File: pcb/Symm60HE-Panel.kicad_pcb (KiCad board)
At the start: 2 copper layers, 175.3 x 233.9 mm, 310 parts

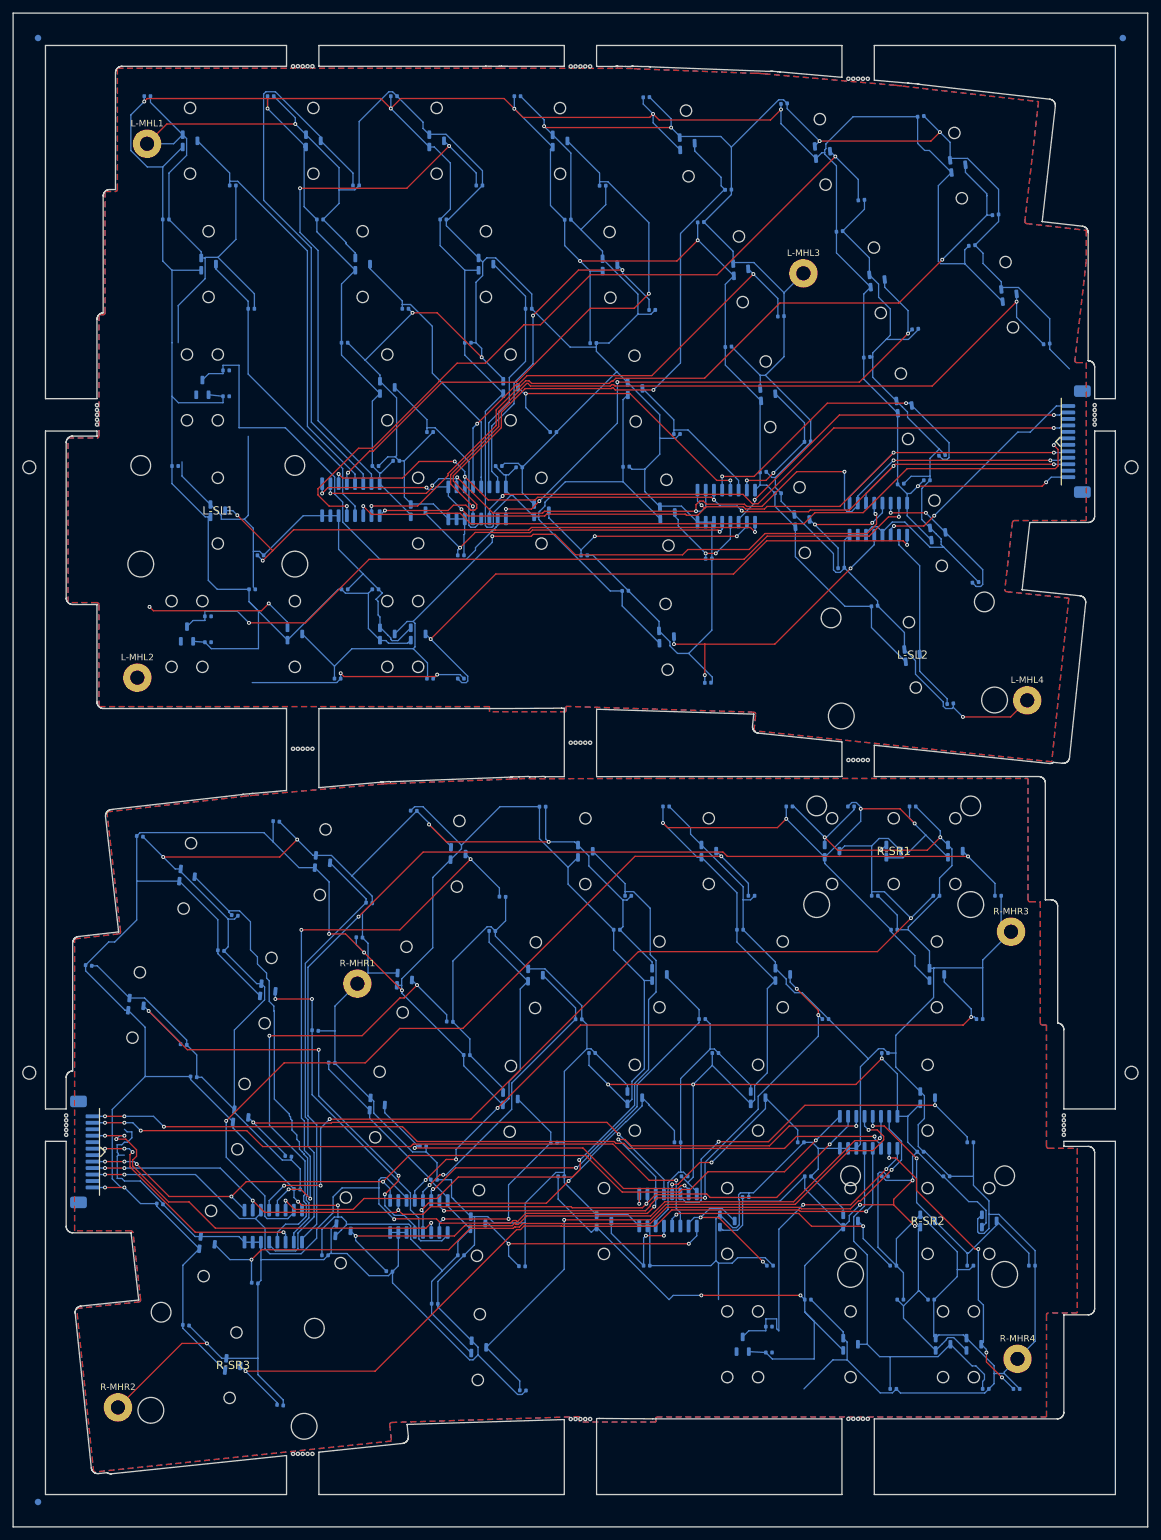
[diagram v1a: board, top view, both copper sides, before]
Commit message: Replace the project with the reorganised T7 tree: ribbon keyboard is production, pogo archived
Production design is now the outward-facing FPC keyboard with per-key
SK6812MINI-E reverse-mount LEDs, a fifth SN74LV4051A mux per half so every
alternate Hall position has its own channel, an SN74AHCT1G125 LED level
shifter, a 50 x 31 mm daughterboard, 1.5 mm POM plates and 3 degree / 7 degree
tent and typing angles. The universal half panel is fully populated (359
placements) with routed NPTH alignment slots for the mutually exclusive
positions, and eight fixed-layout Left/Right PCB pairs are released under
release/layout-pcbs/ with matching BOM, CPL, Gerber ZIP, drill report and DRC.

Reorganise tools/ into cad/, generators/, layouts/, pcb/, pogo/, releases/ and
rendering/ subpackages; add designs/ and layout/ (KLE) trees and per-layout
gallery renders. The Fusion handoff is a fourteen-body reference STEP with
Gateron KS-20 switch and Cherry-profile keycap references and exact BOOMELE,
HRO and XKB models under case/fusion360/models/official/ with provenance.

The Neo-style pogo variant, its Mill-Max vendor models, the Fusion setup
script and the pogo release packages are archived as design history and
marked DO-NOT-ORDER. Their restored BOM snapshots had reintroduced the wrong
mux part C7792; corrected to C128414 / SN74LV4051ADR and their checksum lists
and archives rebuilt.

Co-Authored-By: Claude Opus 5 <noreply@anthropic.com>
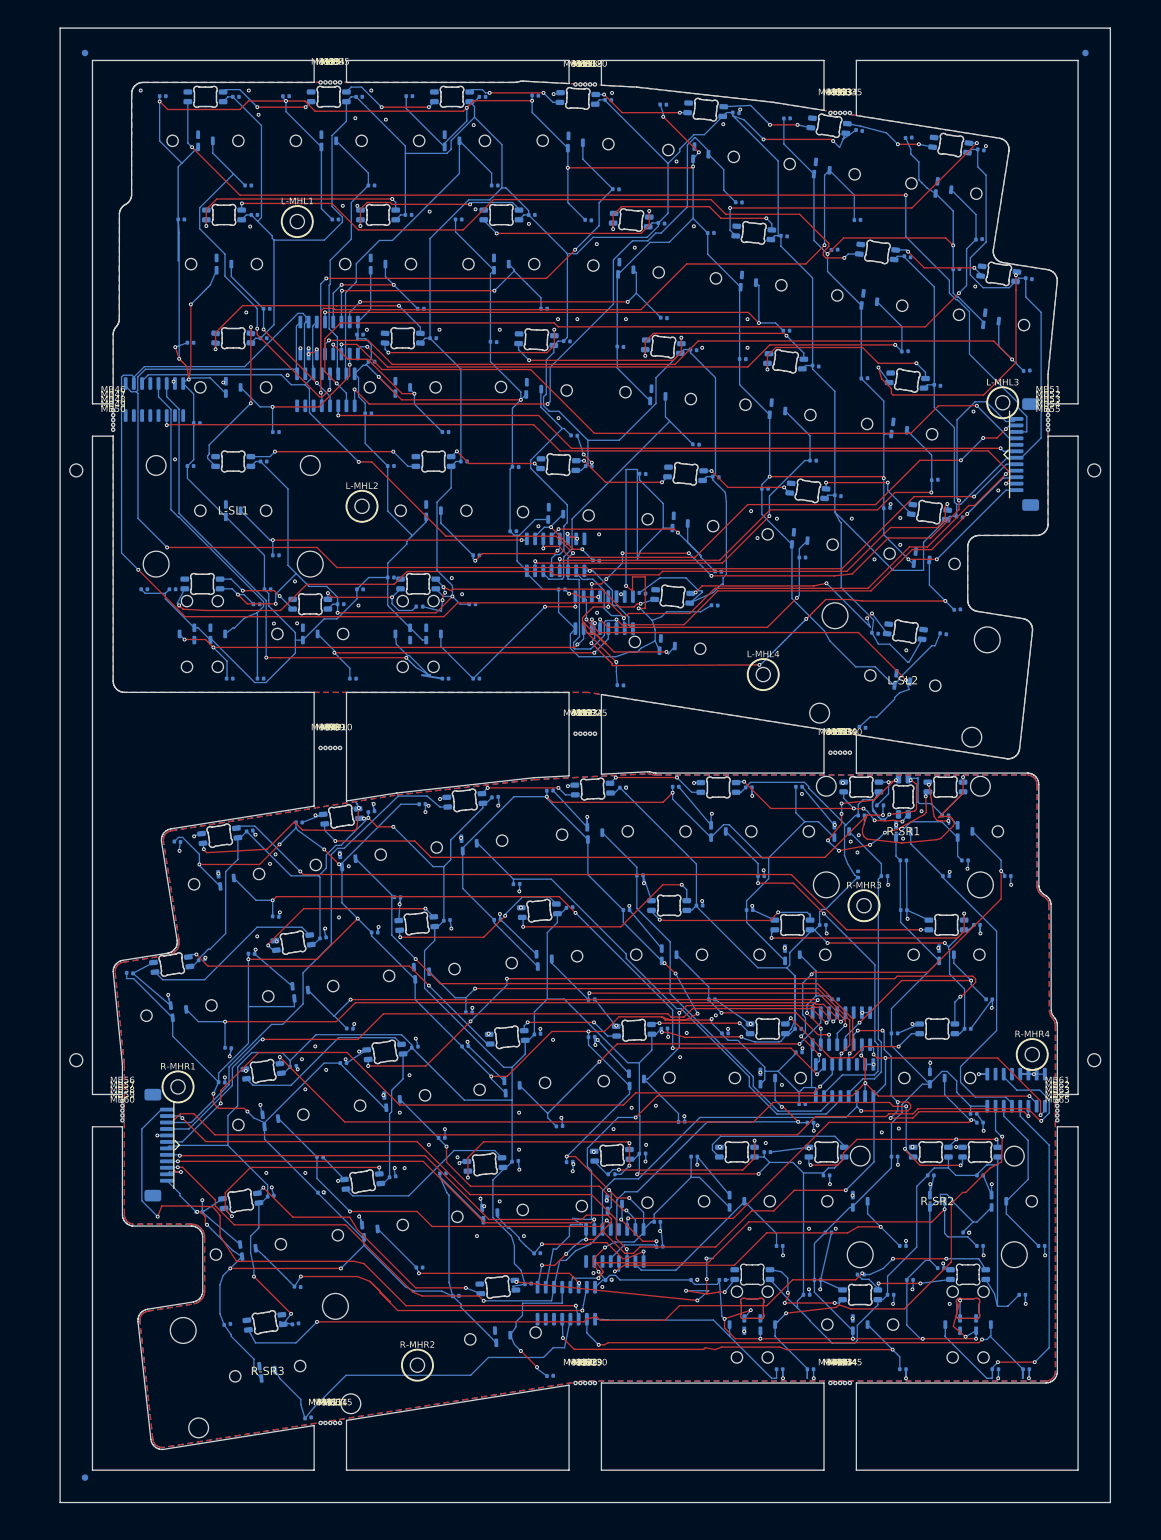
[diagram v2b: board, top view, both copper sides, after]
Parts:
- removed L-KML15N, L-KML15S, L-KML27A, L-KML27N, R-KMR30A, R-KMR30N: MX_MECHANICAL_ONLY, HE_KEY_MECHANICAL_ONLY
- added L-AML5: SN74LV4051A, Symm60HE_Project:AM1_SOIC-16_3.9x9.9mm_P1.27mm, B.Cu at (5.92, 49.5)
- added L-CL28A: 100n, Symm60HE_Project:C1_C_0402_1005Metric, B.Cu at (8.71, 78.8)
- added L-CL28B: 4.7n, Symm60HE_Project:C1_C_0402_1005Metric, B.Cu at (22.3, 92.6)
- added L-CML5: 100n, Symm60HE_Project:C1_C_0402_1005Metric, B.Cu at (12.5, 53.1)
- added L-CRGBL1: 100n, Symm60HE_Project:C1_C_0402_1005Metric, B.Cu at (18.5, 2.73)
- added L-CRGBL10: 100n, Symm60HE_Project:C1_C_0402_1005Metric, B.Cu at (64.2, 21.0)
- added L-CRGBL11: 100n, Symm60HE_Project:C1_C_0402_1005Metric, B.Cu at (45.2, 21.0)
- added L-CRGBL12: 100n, Symm60HE_Project:C1_C_0402_1005Metric, B.Cu at (21.4, 21.0)
- added L-CRGBL13: 100n, Symm60HE_Project:C1_C_0402_1005Metric, B.Cu at (122.3, 27.4)
- added L-CRGBL14: 100n, Symm60HE_Project:C1_C_0402_1005Metric, B.Cu at (141.0, 30.8)
- added L-CRGBL15: 100n, Symm60HE_Project:C1_C_0402_1005Metric, B.Cu at (126.9, 47.3)
- added L-CRGBL16: 100n, Symm60HE_Project:C1_C_0402_1005Metric, B.Cu at (108.1, 44.3)
- added L-CRGBL17: 100n, Symm60HE_Project:C1_C_0402_1005Metric, B.Cu at (89.2, 41.8)
- added L-CRGBL18: 100n, Symm60HE_Project:C1_C_0402_1005Metric, B.Cu at (69.6, 40.5)
- added L-CRGBL19: 100n, Symm60HE_Project:C1_C_0402_1005Metric, B.Cu at (49.0, 40.0)
- added L-CRGBL2: 100n, Symm60HE_Project:C1_C_0402_1005Metric, B.Cu at (37.6, 2.73)
- added L-CRGBL20: 100n, Symm60HE_Project:C1_C_0402_1005Metric, B.Cu at (22.8, 40.0)
- added L-CRGBL21: 100n, Symm60HE_Project:C1_C_0402_1005Metric, B.Cu at (22.8, 59.1)
- added L-CRGBL22: 100n, Symm60HE_Project:C1_C_0402_1005Metric, B.Cu at (53.8, 59.1)
- added L-CRGBL23: 100n, Symm60HE_Project:C1_C_0402_1005Metric, B.Cu at (73.0, 59.8)
- added L-CRGBL24: 100n, Symm60HE_Project:C1_C_0402_1005Metric, B.Cu at (92.7, 61.5)
- added L-CRGBL25: 100n, Symm60HE_Project:C1_C_0402_1005Metric, B.Cu at (111.5, 64.4)
- added L-CRGBL26: 100n, Symm60HE_Project:C1_C_0402_1005Metric, B.Cu at (130.3, 67.6)
- added L-CRGBL27: 100n, Symm60HE_Project:C1_C_0402_1005Metric, B.Cu at (21.7, 81.1)
- added L-CRGBL29: 100n, Symm60HE_Project:C1_C_0402_1005Metric, B.Cu at (55.1, 81.1)
- added L-CRGBL3: 100n, Symm60HE_Project:C1_C_0402_1005Metric, B.Cu at (56.6, 2.73)
- added L-CRGBL30: 100n, Symm60HE_Project:C1_C_0402_1005Metric, B.Cu at (81.3, 79.4)
- added L-CRGBL31: 100n, Symm60HE_Project:C1_C_0402_1005Metric, B.Cu at (117.3, 85.6)
- added L-CRGBL33: 100n, Symm60HE_Project:C1_C_0402_1005Metric, B.Cu at (34.7, 81.1)
- added L-CRGBL4: 100n, Symm60HE_Project:C1_C_0402_1005Metric, B.Cu at (76.0, 3.22)
- added L-CRGBL5: 100n, Symm60HE_Project:C1_C_0402_1005Metric, B.Cu at (95.8, 5.21)
- added L-CRGBL6: 100n, Symm60HE_Project:C1_C_0402_1005Metric, B.Cu at (114.8, 7.93)
- added L-CRGBL7: 100n, Symm60HE_Project:C1_C_0402_1005Metric, B.Cu at (133.6, 10.9)
- added L-CRGBL8: 100n, Symm60HE_Project:C1_C_0402_1005Metric, B.Cu at (103.2, 24.2)
- added L-CRGBL9: 100n, Symm60HE_Project:C1_C_0402_1005Metric, B.Cu at (84.3, 22.3)
- added L-DL1: SK6812MINI-E, Symm60HE_Project:SK6812MINI-E_ReverseMount, B.Cu at (13.8, 2.73)
- added L-DL10: SK6812MINI-E, Symm60HE_Project:SK6812MINI-E_ReverseMount, B.Cu at (59.5, 21.0)
- added L-DL11: SK6812MINI-E, Symm60HE_Project:SK6812MINI-E_ReverseMount, B.Cu at (40.5, 21.0)
- added L-DL12: SK6812MINI-E, Symm60HE_Project:SK6812MINI-E_ReverseMount, B.Cu at (16.7, 21.0)
- added L-DL13: SK6812MINI-E, Symm60HE_Project:SK6812MINI-E_ReverseMount, B.Cu at (117.6, 26.7)
- added L-DL14: SK6812MINI-E, Symm60HE_Project:SK6812MINI-E_ReverseMount, B.Cu at (136.4, 30.1)
- added L-DL15: SK6812MINI-E, Symm60HE_Project:SK6812MINI-E_ReverseMount, B.Cu at (122.3, 46.6)
- added L-DL16: SK6812MINI-E, Symm60HE_Project:SK6812MINI-E_ReverseMount, B.Cu at (103.5, 43.6)
- added L-DL17: SK6812MINI-E, Symm60HE_Project:SK6812MINI-E_ReverseMount, B.Cu at (84.6, 41.3)
- added L-DL18: SK6812MINI-E, Symm60HE_Project:SK6812MINI-E_ReverseMount, B.Cu at (65.0, 40.2)
- added L-DL19: SK6812MINI-E, Symm60HE_Project:SK6812MINI-E_ReverseMount, B.Cu at (44.3, 40.0)
- added L-DL2: SK6812MINI-E, Symm60HE_Project:SK6812MINI-E_ReverseMount, B.Cu at (32.9, 2.73)
- added L-DL20: SK6812MINI-E, Symm60HE_Project:SK6812MINI-E_ReverseMount, B.Cu at (18.1, 40.0)
- added L-DL21: SK6812MINI-E, Symm60HE_Project:SK6812MINI-E_ReverseMount, B.Cu at (18.1, 59.1)
- added L-DL22: SK6812MINI-E, Symm60HE_Project:SK6812MINI-E_ReverseMount, B.Cu at (49.1, 59.1)
- added L-DL23: SK6812MINI-E, Symm60HE_Project:SK6812MINI-E_ReverseMount, B.Cu at (68.3, 59.6)
- added L-DL24: SK6812MINI-E, Symm60HE_Project:SK6812MINI-E_ReverseMount, B.Cu at (88.0, 61.0)
- added L-DL25: SK6812MINI-E, Symm60HE_Project:SK6812MINI-E_ReverseMount, B.Cu at (106.9, 63.6)
- added L-DL26: SK6812MINI-E, Symm60HE_Project:SK6812MINI-E_ReverseMount, B.Cu at (125.7, 66.9)
- added L-DL27: SK6812MINI-E, Symm60HE_Project:SK6812MINI-E_ReverseMount, B.Cu at (13.3, 78.0)
- added L-DL29: SK6812MINI-E, Symm60HE_Project:SK6812MINI-E_ReverseMount, B.Cu at (46.7, 78.0)
- added L-DL3: SK6812MINI-E, Symm60HE_Project:SK6812MINI-E_ReverseMount, B.Cu at (51.9, 2.73)
- added L-DL30: SK6812MINI-E, Symm60HE_Project:SK6812MINI-E_ReverseMount, B.Cu at (86.0, 79.9)
- added L-DL31: SK6812MINI-E, Symm60HE_Project:SK6812MINI-E_ReverseMount, B.Cu at (122.0, 85.4)
- added L-DL33: SK6812MINI-E, Symm60HE_Project:SK6812MINI-E_ReverseMount, B.Cu at (30.0, 81.1)
- added L-DL4: SK6812MINI-E, Symm60HE_Project:SK6812MINI-E_ReverseMount, B.Cu at (71.4, 2.98)
- added L-DL5: SK6812MINI-E, Symm60HE_Project:SK6812MINI-E_ReverseMount, B.Cu at (91.1, 4.72)
- added L-DL6: SK6812MINI-E, Symm60HE_Project:SK6812MINI-E_ReverseMount, B.Cu at (110.2, 7.19)
- added L-DL7: SK6812MINI-E, Symm60HE_Project:SK6812MINI-E_ReverseMount, B.Cu at (129.0, 10.2)
- added L-DL8: SK6812MINI-E, Symm60HE_Project:SK6812MINI-E_ReverseMount, B.Cu at (98.5, 23.8)
- added L-DL9: SK6812MINI-E, Symm60HE_Project:SK6812MINI-E_ReverseMount, B.Cu at (79.6, 21.8)
- added L-HEL28: MT9102ET, HE_KEY_1.50u, B.Cu at (15.7, 85.7)
- added L-RBPL29: 0R_DNP, Symm60HE_Project:R3_R_0402_1005Metric, B.Cu at (46.9, 81.5)
- added R-AMR5: SN74LV4051A, Symm60HE_Project:AM1_SOIC-16_3.9x9.9mm_P1.27mm, B.Cu at (139.1, 156.2)
- added R-CMR5: 100n, Symm60HE_Project:C1_C_0402_1005Metric, B.Cu at (132.5, 159.9)
- added R-CR31A: 100n, Symm60HE_Project:C1_C_0402_1005Metric, B.Cu at (93.7, 185.5)
- added R-CR31B: 4.7n, Symm60HE_Project:C1_C_0402_1005Metric, B.Cu at (107.3, 199.3)
- added R-CRGBR1: 100n, Symm60HE_Project:C1_C_0402_1005Metric, B.Cu at (58.6, 110.9)
- added R-CRGBR10: 100n, Symm60HE_Project:C1_C_0402_1005Metric, B.Cu at (90.2, 127.7)
- added R-CRGBR11: 100n, Symm60HE_Project:C1_C_0402_1005Metric, B.Cu at (70.1, 128.0)
- added R-CRGBR12: 100n, Symm60HE_Project:C1_C_0402_1005Metric, B.Cu at (51.1, 130.0)
- added R-CRGBR13: 100n, Symm60HE_Project:C1_C_0402_1005Metric, B.Cu at (32.0, 132.7)
- added R-CRGBR14: 100n, Symm60HE_Project:C1_C_0402_1005Metric, B.Cu at (13.2, 136.1)
- added R-CRGBR15: 100n, Symm60HE_Project:C1_C_0402_1005Metric, B.Cu at (65.1, 147.6)
- added R-CRGBR16: 100n, Symm60HE_Project:C1_C_0402_1005Metric, B.Cu at (84.7, 146.7)
- added R-CRGBR17: 100n, Symm60HE_Project:C1_C_0402_1005Metric, B.Cu at (105.4, 146.7)
- added R-CRGBR18: 100n, Symm60HE_Project:C1_C_0402_1005Metric, B.Cu at (131.6, 146.7)
- added R-CRGBR19: 100n, Symm60HE_Project:C1_C_0402_1005Metric, B.Cu at (46.2, 149.6)
- added R-CRGBR2: 100n, Symm60HE_Project:C1_C_0402_1005Metric, B.Cu at (78.3, 109.4)
- added R-CRGBR20: 100n, Symm60HE_Project:C1_C_0402_1005Metric, B.Cu at (27.4, 152.5)
- added R-CRGBR21: 100n, Symm60HE_Project:C1_C_0402_1005Metric, B.Cu at (125.9, 169.4)
- added R-CRGBR22: 100n, Symm60HE_Project:C1_C_0402_1005Metric, B.Cu at (109.8, 169.4)
- added R-CRGBR23: 100n, Symm60HE_Project:C1_C_0402_1005Metric, B.Cu at (100.6, 165.8)
- added R-CRGBR24: 100n, Symm60HE_Project:C1_C_0402_1005Metric, B.Cu at (81.3, 166.0)
- added R-CRGBR25: 100n, Symm60HE_Project:C1_C_0402_1005Metric, B.Cu at (61.7, 167.2)
- added R-CRGBR26: 100n, Symm60HE_Project:C1_C_0402_1005Metric, B.Cu at (42.7, 169.6)
- added R-CRGBR27: 100n, Symm60HE_Project:C1_C_0402_1005Metric, B.Cu at (23.9, 172.6)
- added R-CRGBR28: 100n, Symm60HE_Project:C1_C_0402_1005Metric, B.Cu at (63.7, 186.1)
- added R-CRGBR29: 100n, Symm60HE_Project:C1_C_0402_1005Metric, B.Cu at (106.7, 187.8)
- added R-CRGBR3: 100n, Symm60HE_Project:C1_C_0402_1005Metric, B.Cu at (97.8, 109.4)
- added R-CRGBR31: 100n, Symm60HE_Project:C1_C_0402_1005Metric, B.Cu at (140.0, 187.8)
- added R-CRGBR32: 100n, Symm60HE_Project:C1_C_0402_1005Metric, B.Cu at (27.7, 192.3)
- added R-CRGBR33: 100n, Symm60HE_Project:C1_C_0402_1005Metric, B.Cu at (114.7, 122.9)
- added R-CRGBR34: 100n, Symm60HE_Project:C1_C_0402_1005Metric, B.Cu at (133.5, 169.4)
- added R-CRGBR36: 100n, Symm60HE_Project:C1_C_0402_1005Metric, B.Cu at (119.7, 187.8)
- added R-CRGBR4: 100n, Symm60HE_Project:C1_C_0402_1005Metric, B.Cu at (115.2, 113.8)
- added R-CRGBR5: 100n, Symm60HE_Project:C1_C_0402_1005Metric, B.Cu at (128.1, 113.8)
- added R-CRGBR6: 100n, Symm60HE_Project:C1_C_0402_1005Metric, B.Cu at (39.5, 113.2)
- added R-CRGBR7: 100n, Symm60HE_Project:C1_C_0402_1005Metric, B.Cu at (20.7, 116.2)
- added R-CRGBR8: 100n, Symm60HE_Project:C1_C_0402_1005Metric, B.Cu at (133.0, 130.7)
- added R-CRGBR9: 100n, Symm60HE_Project:C1_C_0402_1005Metric, B.Cu at (109.2, 130.7)
- added R-DR1: SK6812MINI-E, Symm60HE_Project:SK6812MINI-E_ReverseMount, B.Cu at (53.9, 111.4)
- added R-DR10: SK6812MINI-E, Symm60HE_Project:SK6812MINI-E_ReverseMount, B.Cu at (85.5, 127.7)
- added R-DR11: SK6812MINI-E, Symm60HE_Project:SK6812MINI-E_ReverseMount, B.Cu at (65.4, 128.5)
- added R-DR12: SK6812MINI-E, Symm60HE_Project:SK6812MINI-E_ReverseMount, B.Cu at (46.5, 130.5)
- added R-DR13: SK6812MINI-E, Symm60HE_Project:SK6812MINI-E_ReverseMount, B.Cu at (27.3, 133.4)
- added R-DR14: SK6812MINI-E, Symm60HE_Project:SK6812MINI-E_ReverseMount, B.Cu at (8.59, 136.8)
- added R-DR15: SK6812MINI-E, Symm60HE_Project:SK6812MINI-E_ReverseMount, B.Cu at (60.4, 148.1)
- added R-DR16: SK6812MINI-E, Symm60HE_Project:SK6812MINI-E_ReverseMount, B.Cu at (80.0, 147.0)
- added R-DR17: SK6812MINI-E, Symm60HE_Project:SK6812MINI-E_ReverseMount, B.Cu at (100.7, 146.7)
- added R-DR18: SK6812MINI-E, Symm60HE_Project:SK6812MINI-E_ReverseMount, B.Cu at (126.9, 146.7)
- added R-DR19: SK6812MINI-E, Symm60HE_Project:SK6812MINI-E_ReverseMount, B.Cu at (41.5, 150.3)
- added R-DR2: SK6812MINI-E, Symm60HE_Project:SK6812MINI-E_ReverseMount, B.Cu at (73.6, 109.7)
- added R-DR20: SK6812MINI-E, Symm60HE_Project:SK6812MINI-E_ReverseMount, B.Cu at (22.7, 153.3)
- added R-DR21: SK6812MINI-E, Symm60HE_Project:SK6812MINI-E_ReverseMount, B.Cu at (125.9, 165.8)
- added R-DR22: SK6812MINI-E, Symm60HE_Project:SK6812MINI-E_ReverseMount, B.Cu at (109.8, 165.8)
- added R-DR23: SK6812MINI-E, Symm60HE_Project:SK6812MINI-E_ReverseMount, B.Cu at (95.9, 165.8)
- added R-DR24: SK6812MINI-E, Symm60HE_Project:SK6812MINI-E_ReverseMount, B.Cu at (76.6, 166.3)
- added R-DR25: SK6812MINI-E, Symm60HE_Project:SK6812MINI-E_ReverseMount, B.Cu at (57.0, 167.7)
- added R-DR26: SK6812MINI-E, Symm60HE_Project:SK6812MINI-E_ReverseMount, B.Cu at (38.1, 170.3)
- added R-DR27: SK6812MINI-E, Symm60HE_Project:SK6812MINI-E_ReverseMount, B.Cu at (19.3, 173.3)
- added R-DR28: SK6812MINI-E, Symm60HE_Project:SK6812MINI-E_ReverseMount, B.Cu at (59.0, 186.6)
- added R-DR29: SK6812MINI-E, Symm60HE_Project:SK6812MINI-E_ReverseMount, B.Cu at (98.3, 184.7)
- added R-DR3: SK6812MINI-E, Symm60HE_Project:SK6812MINI-E_ReverseMount, B.Cu at (93.1, 109.4)
- added R-DR31: SK6812MINI-E, Symm60HE_Project:SK6812MINI-E_ReverseMount, B.Cu at (131.7, 184.7)
- added R-DR32: SK6812MINI-E, Symm60HE_Project:SK6812MINI-E_ReverseMount, B.Cu at (23.0, 192.1)
- added R-DR33: SK6812MINI-E, Symm60HE_Project:SK6812MINI-E_ReverseMount, B.Cu at (121.7, 110.9)
- added R-DR34: SK6812MINI-E, Symm60HE_Project:SK6812MINI-E_ReverseMount, B.Cu at (133.5, 165.8)
- added R-DR36: SK6812MINI-E, Symm60HE_Project:SK6812MINI-E_ReverseMount, B.Cu at (115.0, 187.8)
- added R-DR4: SK6812MINI-E, Symm60HE_Project:SK6812MINI-E_ReverseMount, B.Cu at (115.2, 109.4)
- added R-DR5: SK6812MINI-E, Symm60HE_Project:SK6812MINI-E_ReverseMount, B.Cu at (128.1, 109.4)
- added R-DR6: SK6812MINI-E, Symm60HE_Project:SK6812MINI-E_ReverseMount, B.Cu at (34.8, 113.9)
- added R-DR7: SK6812MINI-E, Symm60HE_Project:SK6812MINI-E_ReverseMount, B.Cu at (16.0, 116.9)
- added R-DR8: SK6812MINI-E, Symm60HE_Project:SK6812MINI-E_ReverseMount, B.Cu at (128.3, 130.7)
- added R-DR9: SK6812MINI-E, Symm60HE_Project:SK6812MINI-E_ReverseMount, B.Cu at (104.5, 130.7)
- added R-HER31: MT9102ET, HE_KEY_1.50u, B.Cu at (100.7, 192.4)
- added R-RBPR24: 0R_DNP, Symm60HE_Project:R3_R_0402_1005Metric, B.Cu at (76.6, 169.2)
- added R-RBPR31: 0R_DNP, Symm60HE_Project:R3_R_0402_1005Metric, B.Cu at (115.1, 184.7)
- added R-RBPR5: 0R_DNP, Symm60HE_Project:R3_R_0402_1005Metric, B.Cu at (118.1, 112.2)
- L-HEL15: footprint HE_SHARED_MIDPOINT -> HE_KEY_1.75u
- L-HEL27, R-HER30: footprint HE_SHARED_MIDPOINT -> HE_KEY_1.00u
- L-MHL1, L-MHL2, L-MHL3, L-MHL4, R-MHR1, R-MHR2, R-MHR3, R-MHR4: value M2 -> M2_NPTH; footprint Symm60HE_Project:MountingHole_2.2mm_M2_Pad -> Symm60HE_Project:MountingHole_2.2mm_M2_NPTH
- moved R-AMR1 91.1 mm to (112.6, 154.7), turned to -90 degrees
- moved R-CMR1 77.3 mm to (106.0, 158.4)
- moved R-AMR2 71.4 mm to (112.1, 146.7), turned to -90 degrees
- moved R-CMR2 60.9 mm to (105.5, 150.4)
- moved L-CML4 58.9 mm to (68.9, 78.9)
- moved R-AMR4 53.7 mm to (69.6, 189.1)
- moved R-CMR4 52.1 mm to (76.1, 185.6)
- moved R-MHR4 47.1 mm to (141.6, 150.7)
- moved R-MHR2 46.7 mm to (46.6, 198.7)
- moved L-AML4 44.8 mm to (75.4, 82.4), turned to -90 degrees
- moved L-MHL2 43.7 mm to (38.0, 66.0)
- moved L-CML3 41.3 mm to (61.4, 69.9)
- moved L-MHL4 41.0 mm to (100.0, 92.0)
- moved L-MHL3 36.7 mm to (137.0, 50.0)
- moved L-AML2 34.2 mm to (32.9, 40.0)
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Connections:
- L-CL30B pad 1: /L/HE_L28 -> /L/HE_L33
- L-HEL30 pad 3: /L/HE_L28 -> /L/HE_L33
- L-JL1 pad 11: /L/GND -> /L/ADC_L5
- L-JL1 pad 3: /L/GND -> /L/RGB_L
- L-JL1 pad 7: /L/GND -> /L/VBUS
- R-CR26B pad 1: /R/HE_R25 -> /R/HE_R34
- R-CR33B pad 1: /R/HE_R30 -> /R/HE_R36
- R-CR4B pad 1: /R/HE_R04 -> /R/HE_R33
- R-HER26 pad 3: /R/HE_R25 -> /R/HE_R34
- R-HER33 pad 3: /R/HE_R30 -> /R/HE_R36
- R-HER4 pad 3: /R/HE_R04 -> /R/HE_R33
- R-JR1 pad 10: /R/GND -> /R/RGB_R
- R-JR1 pad 2: /R/GND -> /R/ADC_R5
- R-JR1 pad 6: /R/GND -> /R/VBUS
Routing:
- net /L/GND: track 1037.8 -> 16.4 mm, vias 12 -> 69
- net /R/GND: track 1151.2 -> 361.1 mm, vias 8 -> 177
- net /L/VBUS: track 0.00 -> 770.8 mm, vias 0 -> 6
- net /R/VBUS: track 0.00 -> 757.4 mm, vias 0 -> 13
- net /L/RGB_L: track 0.00 -> 166.7 mm, vias 0 -> 2
- net /R/ADC_R5: track 0.00 -> 162.2 mm, vias 0 -> 2
- net /L/ADC_L5: track 0.00 -> 138.4 mm, vias 0 -> 2
- net /L/RGB_L_26: track 0.00 -> 131.6 mm, vias 0 -> 2
- net /R/RGB_R_05: track 0.00 -> 123.6 mm, vias 0 -> 3
- net /R/RGB_R_20: track 0.00 -> 123.0 mm, vias 0 -> 4
- net /R/RGB_R_31: track 0.00 -> 121.7 mm, vias 0 -> 4
- net /R/RGB_R_07: track 0.00 -> 113.8 mm, vias 0 -> 2
- net /R/RGB_R_18: track 0.00 -> 109.7 mm, vias 0 -> 4
- net /R/HE_R04: track 155.4 -> 46.5 mm, vias 4 -> 0
- net /L/RGB_L_12: track 0.00 -> 106.3 mm, vias 0 -> 2
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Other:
- board size 175.3 x 233.9 mm -> 162.3 x 227.8 mm

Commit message: Move every LED into the switch's south RGB pocket
The reverse-mount SK6812MINI-E sat 7.60 mm north of each key, shining into
the Gateron KS-20's opaque cover rather than its window. All 65 LEDs now sit
5.35 mm south of their key, in the pocket the cover is moulded for, so the
board lights like a Wooting 60HE+ backlight instead of a pass-through for a
transparent cap. Switches install with their RGB pocket toward the user; the
plate cutout and the alignment pins are symmetric, so nothing else changes.

Both halves were re-routed around the new apertures and are fully connected
with no DRC errors: 247 vias on the left (was 251) and 418 on the right (was
393). A handful of GND pads the apertures fence off on both layers reach the
plane through a via inside the pad, so the order checklist now asks for tented
vias. The pours' copies of the apertures moved with the LEDs -- they had been
left behind at the old positions, cutting some 800 mm2 of ground per layer for
openings that were no longer there.

The fixed-layout derivatives needed more than a copy of that work. Each one
restores its close-pair switches' alignment drills to the horizontal axis, and
the masters' new routing ran where those drills land, so the finishing pass
grew a repair loop: give a finding room, route it again, and keep the result
only if nothing got worse -- no new opens, and never a short. A net the router
cannot put back keeps the copper it had. Where a gap is short by microns the
trace is bent clear rather than ripped, because on a board this full a ripped
trace comes back exactly where it was. An LED only returns to its fixed-layout
row when that space is free, and the stabilisers keep the master's angle now
that they no longer have a northern aperture to face. All sixteen boards report
zero DRC and connectivity errors, and the audit checks the pocket window rather
than a nominal offset.

The panel gained the same care: a break row would have drilled through a trace
running along the right half'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
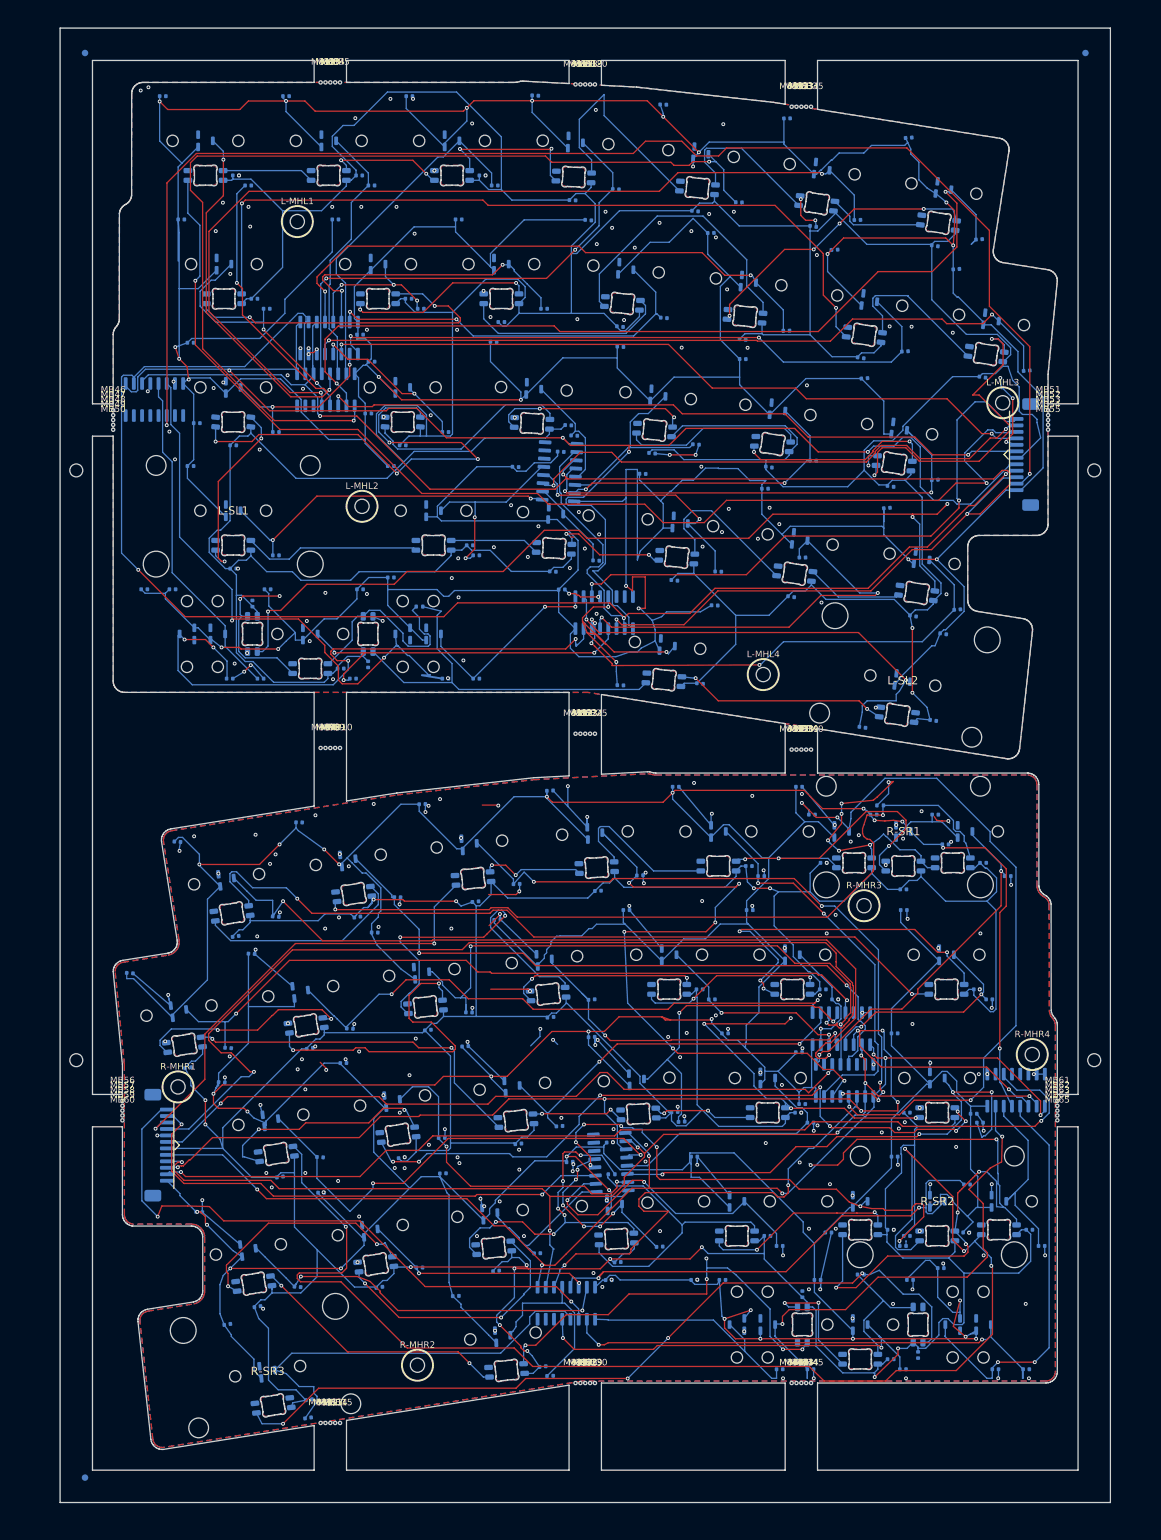
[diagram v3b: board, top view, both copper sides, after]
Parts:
- moved L-CRGBL29 18.6 mm to (38.9, 90.4), turned to -90 degrees
- moved R-CRGBR31 18.6 mm to (123.9, 197.1), turned to -90 degrees
- moved L-CRGBL17 17.2 mm to (82.8, 57.8)
- moved L-CRGBL19 17.2 mm to (44.3, 56.6)
- moved L-CRGBL20 17.2 mm to (18.1, 56.6)
- moved L-CRGBL21 17.2 mm to (18.1, 75.6)
- moved R-CRGBR15 17.2 mm to (62.2, 164.5)
- moved R-CRGBR11 17.2 mm to (67.1, 144.9)
- moved R-CRGBR12 17.2 mm to (48.2, 146.9)
- moved L-CRGBL8 17.2 mm to (96.8, 40.2)
- moved L-CRGBL13 17.2 mm to (115.1, 43.1)
- moved R-CRGBR13 17.2 mm to (29.9, 149.8)
- moved R-CRGBR19 17.2 mm to (44.1, 166.7)
- moved R-CRGBR24 17.2 mm to (77.5, 182.8)
- moved L-CRGBL10 17.2 mm to (59.5, 37.5)
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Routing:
- net /R/GND: track 361.1 -> 205.4 mm
- net /L/+3V3A: track 942.3 -> 1059.3 mm, vias 22 -> 21
- net /R/+3V3A: track 941.8 -> 1042.2 mm, vias 33 -> 27
- net /R/RGB_R_20: track 123.0 -> 208.1 mm
- net /L/ADC_L5: track 138.4 -> 218.5 mm
- net /R/RGB_R_21: track 35.3 -> 100.5 mm, vias 3 -> 6
- net /R/HE_R04: track 46.5 -> 110.2 mm, vias 0 -> 4
- net /R/MUX_A0: track 191.8 -> 254.2 mm, vias 8 -> 9
- net /L/HE_L05: track 98.5 -> 152.0 mm
- net /L/MUX_A0: track 192.4 -> 244.1 mm
- net /R/HE_R02: track 63.9 -> 105.1 mm, vias 0 -> 6
- net /L/HE_L01: track 57.7 -> 94.6 mm, vias 2 -> 3
- net /L/RGB_L_19: track 39.2 -> 74.3 mm, vias 2 -> 4
- net /R/ADC_R2: track 114.2 -> 149.0 mm
- net /L/GND: track 16.4 -> 47.2 mm, vias 69 -> 104
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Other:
- outline, holes or cut-outs redrawn
